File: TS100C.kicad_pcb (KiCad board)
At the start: 4 copper layers, 84 x 10 mm, 50 parts, among them J1 USB-C_Power, J2 OLED_64x32, J3 A, J4 B, Q1 SS8050, Q2 DMP3017SFG, SW1 Setup, U1 USBLC6-2SC6, U2 AP2204R-3.3, U3 FUSB302BMPX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

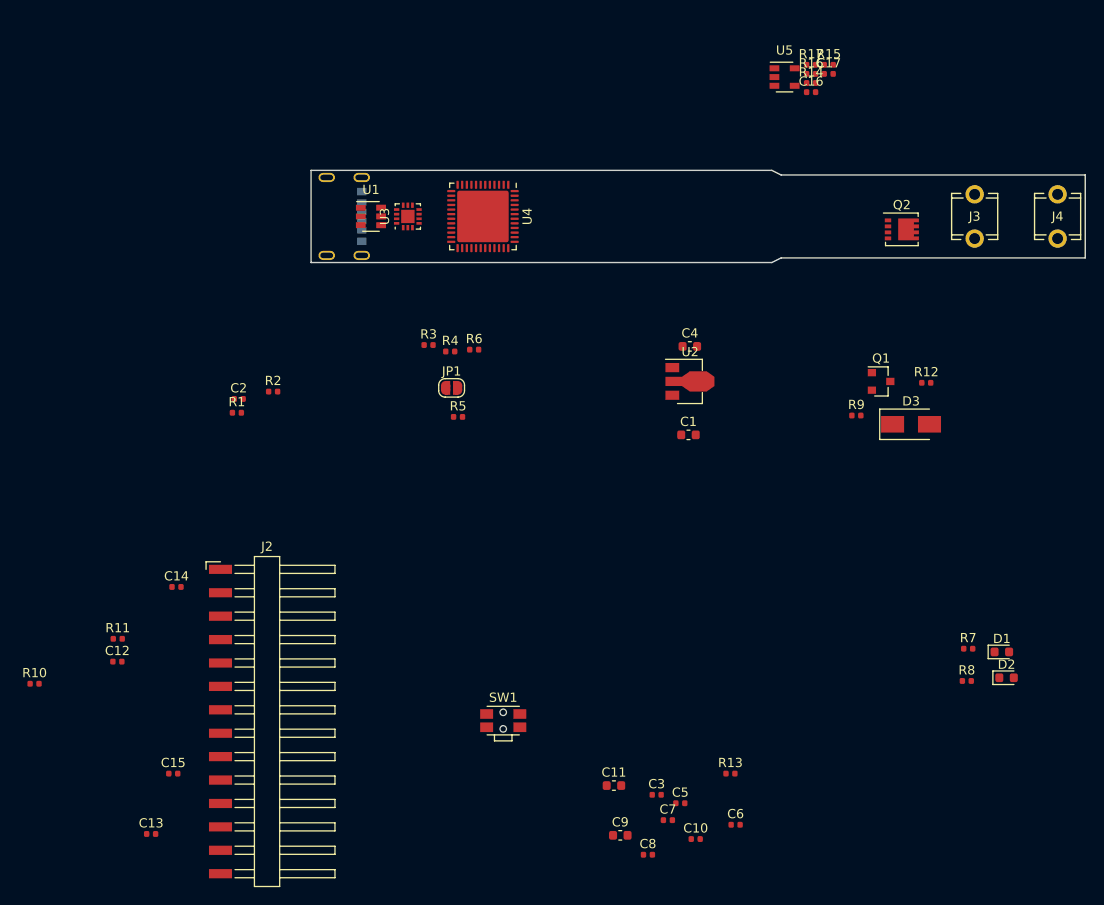
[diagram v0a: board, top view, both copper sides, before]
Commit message: added most parts
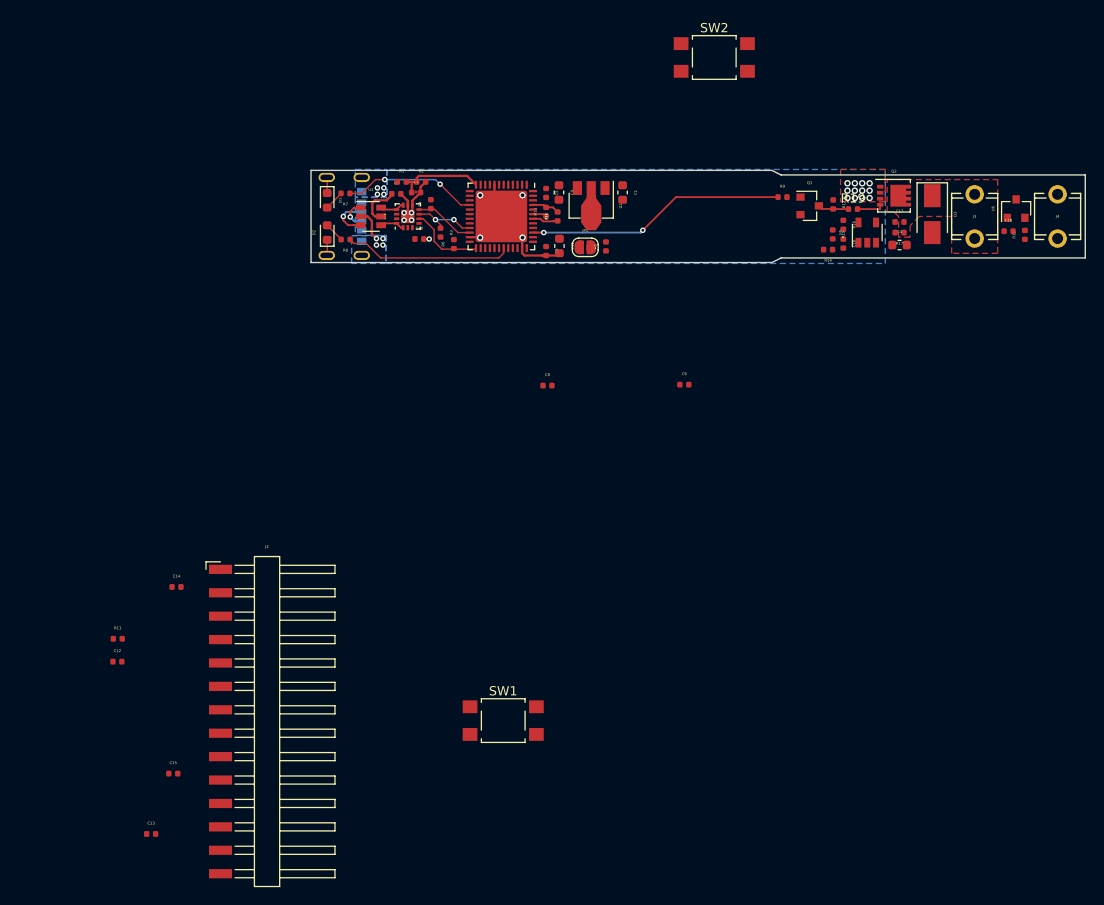
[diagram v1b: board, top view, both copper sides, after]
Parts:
- added C18: 0.1μF, Capacitor_SMD:C_0402_1005Metric, F.Cu at (155.7, 86.6)
- added R18: 1k, Resistor_SMD:R_0402_1005Metric, F.Cu at (157.4, 87.0)
- added R19: 20, Resistor_SMD:R_0402_1005Metric, F.Cu at (138.8, 84.2)
- added SW2: key2, Button_Switch_SMD:SW_SPST_TL3305B, F.Cu at (123.8, 67.8)
- added U6: MCP9700AT-ETT, Package_TO_SOT_SMD:SOT-23, F.Cu at (156.5, 84.2)
- C16: value 10n -> 0.1uF
- C17: value 100n -> 0.1μF
- Q2: footprint Package_SON:Diodes_PowerDI3333-8 -> otter:Diodes_PowerDI3333-8
- R10, R13, R9: value 2kΩ -> 2k
- R12: value 100kΩ -> 10k
- SW1: value Setup -> key1; footprint Button_Switch_SMD:SW_SPST_EVQP7C -> Button_Switch_SMD:SW_SPST_TL3305B
- moved D2 88.1 mm to (81.8, 86.8), turned to 90 degrees
- moved D1 88.1 mm to (81.8, 83.2), turned to 270 degrees
- moved R7 83.7 mm to (83.7, 82.5), turned to 180 degrees
- moved R8 82.7 mm to (83.8, 87.5), turned to 180 degrees
- moved R10 76.1 mm to (106.8, 85.0), turned to 90 degrees
- moved C7 74.1 mm to (89.2, 82.5)
- moved C10 71.7 mm to (91.8, 87.5)
- moved C9 70.1 mm to (106.9, 82.4), turned to 270 degrees
- moved C5 67.8 mm to (105.5, 82.5), turned to 270 degrees
- moved R13 64.1 mm to (105.5, 84.5), turned to 90 degrees
- moved C3 60.2 mm to (105.5, 88.8), turned to 270 degrees
- moved C11 58.8 mm to (107.0, 88.2), turned to 270 degrees
- moved C8 52.1 mm to (105.7, 103.3)
- moved C6 48.1 mm to (120.5, 103.2)
- moved R1 30.8 mm to (89.8, 81.2)
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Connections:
- net APA102_MOSI renamed Net-(U4-Pad17)
- net APA102_SCK renamed Net-(U4-Pad15)
- net TMP renamed TTIP
- net U_OUT renamed UIN
- Q2 pad 4: Net-(Q1-Pad3) -> Net-(Q2-Pad4)
- R9 pad 1: OUT_CTL -> PWM
- U4 pad 10: Net-(U4-Pad10) -> TREF
- U4 pad 16: Net-(U4-Pad16) -> Net-(R7-Pad1)
- U4 pad 38: Net-(R7-Pad1) -> Net-(U4-Pad38)
- U4 pad 39: OLED_PULLUP -> PWM
- U4 pad 45: OUT_CTL -> OLED_PULLUP
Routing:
- net GND: track 0.00 -> 32.2 mm, vias 0 -> 17
- net PWM: track 0.00 -> 28.2 mm, vias 0 -> 2
- net Net-(R8-Pad1): track 0.00 -> 18.2 mm
- net Net-(R7-Pad1): track 0.00 -> 14.8 mm, vias 0 -> 2
- net UIN: track 0.00 -> 10.3 mm
- net INT_N: track 0.00 -> 8.34 mm
- net SCL: track 0.00 -> 7.26 mm, vias 0 -> 2
- net SDA: track 0.00 -> 6.55 mm
- net +3V3: track 0.00 -> 4.86 mm
- net CC2: track 0.00 -> 4.84 mm, vias 0 -> 1
- net Net-(Q1-Pad3): track 0.00 -> 4.28 mm
- net CC1: track 0.00 -> 3.34 mm, vias 0 -> 1
- net OLED_PULLUP: track 0.00 -> 2.98 mm
- net Net-(Q2-Pad4): track 0.00 -> 2.90 mm
- net OLED_SCL: track 0.00 -> 2.80 mm
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- added copper zone on F.Cu, net /OUT
- added copper zone on B.Cu, net GND
- added copper zone on In2.Cu, net GND
- added copper zone on B.Cu, net VBUS
- added copper zone on F.Cu, net VBUS

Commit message: update PCB
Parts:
- J2: footprint Connector_Harwin:Harwin_M20-89014xx_1x14_P2.54mm_Horizontal -> otter:0.69OLED; moved to B.Cu
- SW1, SW2: moved to B.Cu
- moved J2 60.1 mm to (100.4, 85.0), turned to 90 degrees
- moved C12 58.2 mm to (102.5, 94.8)
- moved SW1 57.4 mm to (118.2, 85.0), turned to 270 degrees
- moved C13 55.9 mm to (90.5, 103.6)
- moved C15 55.9 mm to (93.0, 97.0)
- moved C14 47.1 mm to (101.5, 95.0)
- moved R11 43.4 mm to (90.0, 100.4)
- moved SW2 17.5 mm to (126.8, 85.0), turned to 90 degrees
- moved C8 15.0 mm to (120.6, 104.8)
- moved R5 4.30 mm to (108.4, 85.9), turned to 270 degrees
- moved C1 2.00 mm to (114.5, 84.2), turned to 90 degrees
- moved JP1 0.81 mm to (110.3, 87.8), turned to 90 degrees
- moved U2 0.63 mm to (111.0, 83.4), turned to 180 degrees
- moved R10 0.40 mm to (107.1, 85.2)
- moved R13 0.30 mm to (105.8, 84.5)
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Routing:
- net +3V3: track 4.86 -> 65.3 mm, vias 0 -> 17
- net Net-(JP1-Pad2): track 0.00 -> 8.58 mm, vias 0 -> 2
- net GND: track 32.2 -> 38.9 mm, vias 17 -> 31
- net Net-(C16-Pad1): track 0.00 -> 6.39 mm
- net Net-(C16-Pad2): track 0.00 -> 4.30 mm
- net VBUS: track 0.00 -> 3.61 mm, vias 12 -> 31
- net Net-(R17-Pad2): track 0.00 -> 2.52 mm
- net Net-(R18-Pad2): track 0.00 -> 1.36 mm
- net OLED_PULLUP: track 2.98 -> 3.82 mm
- net OLED_SDA: track 1.51 -> 2.08 mm, vias 0 -> 1
- net OLED_SCL: track 2.80 -> 3.19 mm, vias 0 -> 1
- added copper zone on B.Cu, net +3V3
- added copper zone on F.Cu, net +3V3
- added copper zone on In2.Cu, net +3V3
- added copper zone on F.Cu, net GND
- added copper zone on In1.Cu, net VBUS

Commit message: update PCB
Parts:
- removed D1: Status, LED_SMD:LED_0603_1608Metric
- removed D2: Power, LED_SMD:LED_0603_1608Metric
- removed JP1: Boot, Jumper:SolderJumper-2_P1.3mm_Open_RoundedPad1.0x1.5mm
- removed R7, R8: 2k, Resistor_SMD:R_0402_1005Metric
- added J5: DNP, Resistor_SMD:R_0402_1005Metric, F.Cu at (115.9, 85.0)
- added P1: TC2030-CTX, Tag-Connect:TC2030-NL_SMALL, F.Cu at (119.0, 88.0)
- C12, C13, C14, C15, R10, R11, R13: moved to B.Cu
- J1: value USB-C_Power -> USB_C; footprint otter:USB-C_Power -> Connector_USB:USB_C_Receptacle_Amphenol_12401548E4-2A
- SW1, SW2: footprint Button_Switch_SMD:SW_SPST_TL3305B -> Button_Switch_SMD:SW_SPST_PTS810
- U1: value USBLC6-2SC6 -> USBLC6-4SC6
- moved C13 43.4 mm to (128.1, 81.9)
- moved R11 41.9 mm to (128.1, 82.9)
- moved C15 38.7 mm to (128.1, 80.9)
- moved SW2 28.0 mm to (154.8, 85.0)
- moved C14 27.2 mm to (127.8, 88.6), turned to 270 degrees
- moved C12 26.6 mm to (127.8, 86.7), turned to 90 degrees
- moved J2 24.6 mm to (125.0, 85.0)
- moved C6 23.6 mm to (103.0, 87.3)
- moved C8 22.4 mm to (123.2, 82.5), turned to 270 degrees
- moved R13 22.3 mm to (128.1, 83.9), turned to 0 degrees
- moved SW1 22.3 mm to (140.5, 85.0), turned to 0 degrees
- moved R10 21.0 mm to (128.1, 84.9), turned to 0 degrees
- moved C2 11.1 mm to (102.5, 81.6), turned to 270 degrees
- moved R2 9.46 mm to (101.4, 81.6), turned to 270 degrees
- moved R4 8.69 mm to (101.3, 86.2), turned to 180 degrees
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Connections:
- U1 pad 1: CC1 -> USB_N
- U1 pad 4: CC2_P -> CC1
- U1 pad 6: CC1_P -> USB_P
- U3 pad 1: CC2_P -> CC2
- U3 pad 10: CC1_P -> CC1
- U3 pad 11: CC1_P -> CC1
- U3 pad 14: CC2_P -> CC2
- U4 pad 32: Net-(U4-Pad32) -> USB_N
- U4 pad 33: Net-(U4-Pad33) -> USB_P
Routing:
- net Net-(SW2-Pad2): track 0.00 -> 62.6 mm, vias 0 -> 3
- net TREF: track 0.00 -> 55.5 mm, vias 0 -> 2
- net Net-(SW1-Pad2): track 0.00 -> 41.7 mm, vias 0 -> 2
- net TTIP: track 0.00 -> 38.2 mm, vias 0 -> 2
- net nRST: track 0.00 -> 31.1 mm
- net USB_P: track 0.00 -> 28.6 mm, vias 0 -> 2
- net USB_N: track 0.00 -> 26.5 mm, vias 0 -> 1
- net OLED_PULLUP: track 3.82 -> 25.2 mm, vias 0 -> 1
- net Net-(U4-Pad31): track 18.3 -> 0.00 mm
- net OLED_SDA: track 2.08 -> 18.1 mm
- net OLED_SCL: track 3.19 -> 18.2 mm
- net Net-(U4-Pad16): track 14.8 -> 0.00 mm, vias 2 -> 0
- net +3V3: track 65.3 -> 51.7 mm, vias 17 -> 16
- net GND: track 38.9 -> 52.0 mm, vias 31 -> 28
- net CC2: track 4.68 -> 17.7 mm, vias 1 -> 2
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- removed copper zone on In2.Cu, net +3V3
- removed copper zone on B.Cu, net GND
- removed copper zone on B.Cu, net VBUS
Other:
- rule pad_to_mask_clearance: 0.2 -> 0.154

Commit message: finalized PCB
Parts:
- moved J5 0.11 mm to (115.8, 85.0)
- moved R5 0.06 mm to (113.9, 85.0)

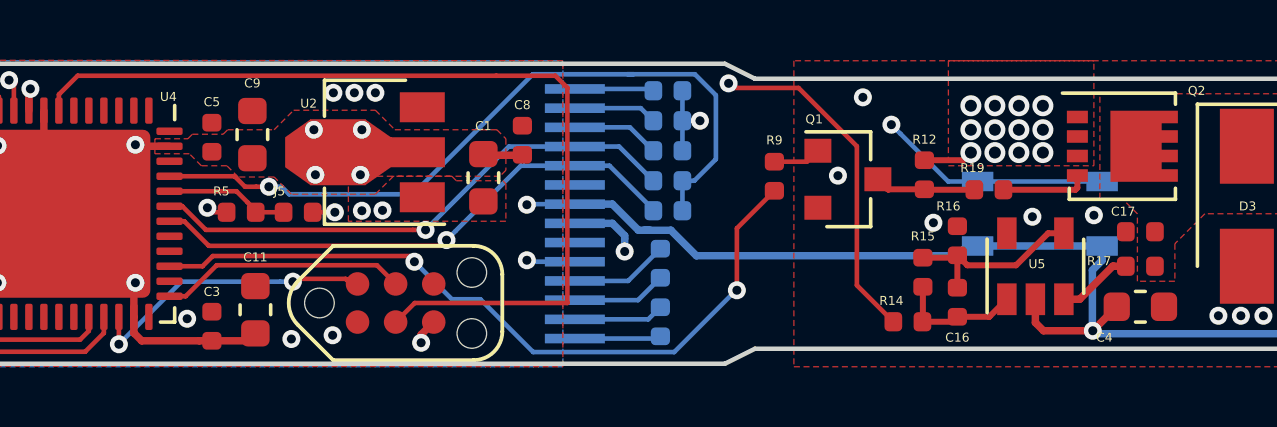
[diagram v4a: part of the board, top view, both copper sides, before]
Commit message: fixed connector error
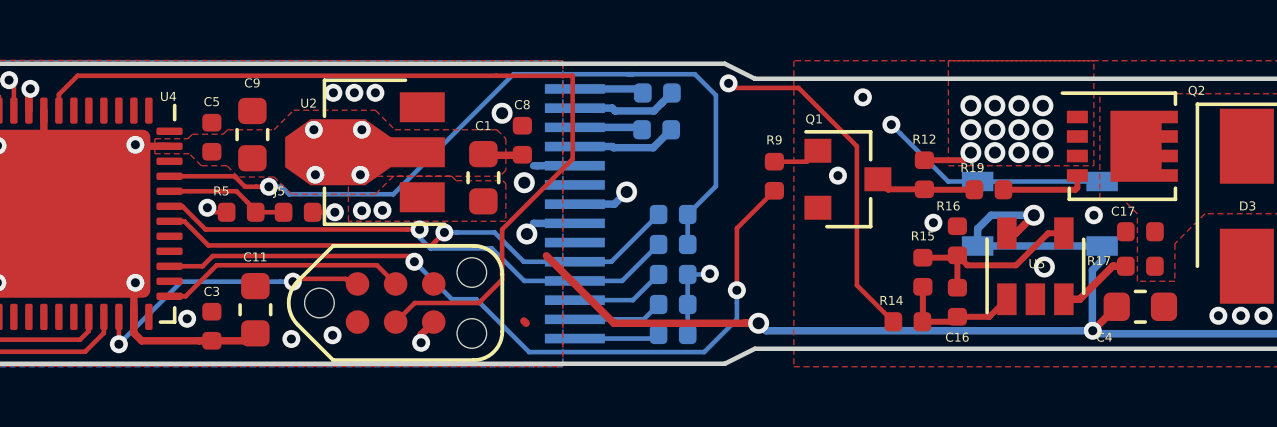
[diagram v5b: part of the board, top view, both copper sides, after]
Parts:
- moved C15 8.13 mm to (128.3, 89.0)
- moved C14 7.63 mm to (127.8, 81.0), turned to 180 degrees
- moved C13 6.13 mm to (128.3, 88.0)
- moved C12 4.45 mm to (127.7, 82.2), turned to 0 degrees
- moved R11 4.13 mm to (128.3, 87.0)
- moved R13 2.13 mm to (128.3, 86.0)
- moved R10 0.22 mm to (128.3, 85.0)
- turned J2 to 270 degrees
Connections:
- U5 pad 2: +3V3 -> GND
- U5 pad 5: GND -> +3V3
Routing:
- net +3V3: track 51.7 -> 58.0 mm, vias 16 -> 19
- net nRST: track 31.1 -> 29.8 mm
- net Net-(C12-Pad1): track 3.16 -> 2.27 mm
- net OLED_PULLUP: track 25.2 -> 26.0 mm
- net PWM: track 25.1 -> 25.7 mm
- net Net-(C14-Pad2): track 2.88 -> 2.32 mm
- net Net-(C14-Pad1): track 3.02 -> 3.52 mm

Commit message: update PCB
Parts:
- J4: footprint otter:Keystone_3621 -> otter:3622TR
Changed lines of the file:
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@@
     (add_net nRST)
+  )
+  (module otter:3622TR (layer F.Cu)
+    (at 161 85)
+    (fp_text reference J4 (at 0 -3.175) (layer F.SilkS)
+      (effects (font (size 1 1) (thickness 0.15)))
+    )
+    (fp_text value B (at 0 -5.08) (layer F.Fab)
+      (effects (font (size 1 1) (thickness 0.15)))
+    )
+    (pad 1 thru_hole rect (at 0 0) (size 5 3.96) (drill 1.7) (layers *.Cu *.Mask)
+      (net 1 GND))
   )
   (module Capacitor_SMD:C_0402_1005Metric (layer F.Cu)
@@
     )
   )
-  (module otter:Keystone_3621 (layer F.Cu)
-    (at 161 85)
-    (fp_text reference J4 (at -2.275 -2.775) (layer F.SilkS)
-      (effects (font (size 0.3 0.3) (thickness 0.05)))
-    )
-    (fp_text value B (at 0 -4.5) (layer F.Fab)
-      (effects (font (size 1 1) (thickness 0.15)))
-    )
-    (fp_line (start 1.25 -2) (end 2.5 -2) (layer F.SilkS) (width 0.15))
-    (fp_line (start -2.5 -2) (end -1.25 -2) (layer F.SilkS) (width 0.15))
-    (fp_line (start -1.25 2) (end -2.5 2) (layer F.SilkS) (width 0.15))
-    (fp_line (start 1.25 2) (end 2.5 2) (layer F.SilkS) (width 0.15))
-    (fp_line (start 1.5 -2.5) (end 2.5 -2.5) (layer F.SilkS) (width 0.15))
-    (fp_line (start 2.5 2.5) (end 1.5 2.5) (layer F.SilkS) (width 0.15))
-    (fp_line (start -1.5 -2.5) (end -2.5 -2.5) (layer F.SilkS) (width 0.15))
-    (fp_line (start 2.5 2.5) (end 2.5 -2.5) (layer F.SilkS) (width 0.15))
-    (fp_line (start -2.5 2.5) (end -1.5 2.5) (layer F.SilkS) (width 0.15))
-    (fp_line (start -2.5 -2.5) (end -2.5 2.5) (layer F.SilkS) (width 0.15))
-    (pad 1 thru_hole circle (at 0 2.4) (size 2 2) (drill 1.19) (layers *.Cu *.Mask)
-      (net 1 GND))
-    (pad 1 thru_hole circle (at 0 -2.4) (size 2 2) (drill 1.19) (layers *.Cu *.Mask)
-      (net 1 GND))
-    (model /home/janhenrik/Downloads/keystone-PN3621.STEP
-      (offset (xyz 0 0 0.2))
-      (scale (xyz 1 1 1))
-      (rotate (xyz -90 0 90))
-    )
-  )

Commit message: update pcb
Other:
- board text added: "DFU ^"

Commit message: updated files
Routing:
- net +3V3: track 58.0 -> 62.2 mm
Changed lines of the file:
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@@
-(kicad_pcb (version 20171130) (host pcbnew "(6.0.0-rc1-dev-1-g01c5bdfb8)")
+(kicad_pcb (version 20171130) (host pcbnew 5.0.1)
   (general
     (thickness 1.6)
     (drawings 9)
-    (tracks 506)
+    (tracks 509)
     (zones 0)
     (modules 52)
@@
   )
   (setup
-    (last_trace_width 0.154)
+    (last_trace_width 0.25)
     (user_trace_width 0.154)
     (user_trace_width 0.2)
@@
     (tags capacitor)
     (attr smd)
-    (fp_text reference C12 (at 0.525 0.75) (layer B.SilkS)
+    (fp_text reference C12 (at 1.55 0) (layer B.SilkS)
       (effects (font (size 0.4 0.4) (thickness 0.1)) (justify mirror))
     )
@@
     (tags capacitor)
     (attr smd)
-    (fp_text reference C13 (at 1.225 0 90) (layer B.SilkS)
+    (fp_text reference C13 (at 1.55 0 180) (layer B.SilkS)
       (effects (font (size 0.4 0.4) (thickness 0.1)) (justify mirror))
     )
@@
     (tags capacitor)
     (attr smd)
-    (fp_text reference C14 (at -0.525 -0.75 180) (layer B.SilkS)
+    (fp_text reference C14 (at -1.55 -0.025 180) (layer B.SilkS)
       (effects (font (size 0.4 0.4) (thickness 0.1)) (justify mirror))
     )
@@
     (tags capacitor)
     (attr smd)
-    (fp_text reference C15 (at 1.225 -0.025 90) (layer B.SilkS)
+    (fp_text reference C15 (at 1.55 -0.025 180) (layer B.SilkS)
       (effects (font (size 0.4 0.4) (thickness 0.1)) (justify mirror))
     )
@@
     (tags resistor)
     (attr smd)
-    (fp_text reference R10 (at 1.2 0 90) (layer B.SilkS)
+    (fp_text reference R10 (at 1.55 0 180) (layer B.SilkS)
       (effects (font (size 0.4 0.4) (thickness 0.1)) (justify mirror))
     )
@@
     (tags resistor)
     (attr smd)
-    (fp_text reference R11 (at 1.2 0 90) (layer B.SilkS)
+    (fp_text reference R11 (at 1.525 0 180) (layer B.SilkS)
       (effects (font (size 0.4 0.4) (thickness 0.1)) (justify mirror))
     )
@@
     (tags resistor)
     (attr smd)
-    (fp_text reference R13 (at 1.2 0 90) (layer B.SilkS)
+    (fp_text reference R13 (at 1.55 0) (layer B.SilkS)
       (effects (font (size 0.4 0.4) (thickness 0.1)) (justify mirror))
     )
@@
   (segment (start 116.37 84.95) (end 117 84.95) (width 0.154) (layer F.Cu) (net 10))
   (via (at 117 84.95) (size 0.6) (drill 0.3) (layers F.Cu B.Cu) (net 10))
+  (segment (start 104.6125 87.75) (end 104.3125 88.05) (width 0.25) (layer F.Cu) (net 10))
+  (segment (start 102.3 88.05) (end 101.7 87.45) (width 0.25) (layer F.Cu) (net 10))
+  (segment (start 104.3125 88.05) (end 102.3 88.05) (width 0.25) (layer F.Cu) (net 10))
+  (segment (start 111.4875 82.25) (end 110.8 81.5625) (width 0.25) (layer F.Cu) (net 10))
   (via (at 102.999992 84.95) (size 0.6) (drill 0.3) (layers F.Cu B.Cu) (net 11))
   (segment (start 102.699993 84.650001) (end 102.999992 84.95) (width 0.154) (layer F.Cu) (net 11))
@@
   (segment (start 119.05 81.5) (end 119.75 80.8) (width 0.154) (layer In1.Cu) (net 57))
   (segment (start 119.75 80.8) (end 129.25 80.8) (width 0.154) (layer In1.Cu) (net 57))
-  (segment (start 129.25 80.8) (end 129.4 80.8) (width 0.154) (layer In1.Cu) (net 57))
   (segment (start 134.300001 81.418989) (end 134.6 81.11899) (width 0.154) (layer In1.Cu) (net 57))
   (segment (start 129.25 80.8) (end 129.868989 81.418989) (width 0.154) (layer In1.Cu) (net 57))
